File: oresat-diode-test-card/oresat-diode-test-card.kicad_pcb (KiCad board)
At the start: 4 copper layers, 99.8 x 94.6 mm, 123 parts, among them J6 J-SAMTEC-TFM-120-X1-XXX-D-RA, J7 ORESAT-DEBUG-CONNECTOR-ALL, Q1 DMP2240UDM, Q2 DMP3050LVT-7, Q4 DMP3050LVT-7, Q7 MOSFET-PCH-SOT23-6, Q8 PMV45EN, Q9 PMV45EN, U1 TCAN330, U10 TPS62111RSA, U11 MIC842LYC5, U12 MIC842LYC5, U2 MAX7310, U3 TS5A21366DCUR, U4 TLV6001DCK, U501 TLV6001DCK, U6 MAX4211, U7 STM32F091C, U8 NX3L4051-Q100, U9 TLV6001DCK, X2 CRYSTAL-WITH-GND

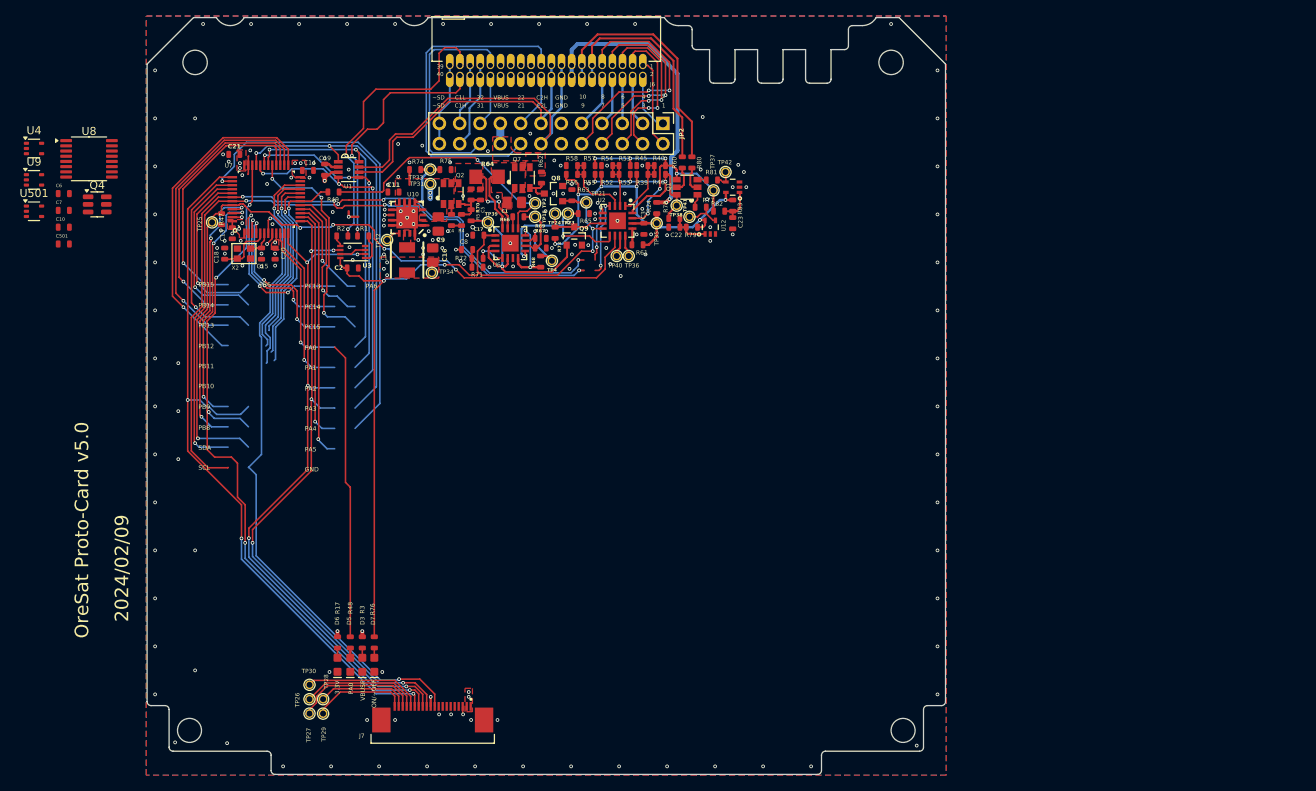
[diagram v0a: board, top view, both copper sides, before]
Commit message: started layout of components
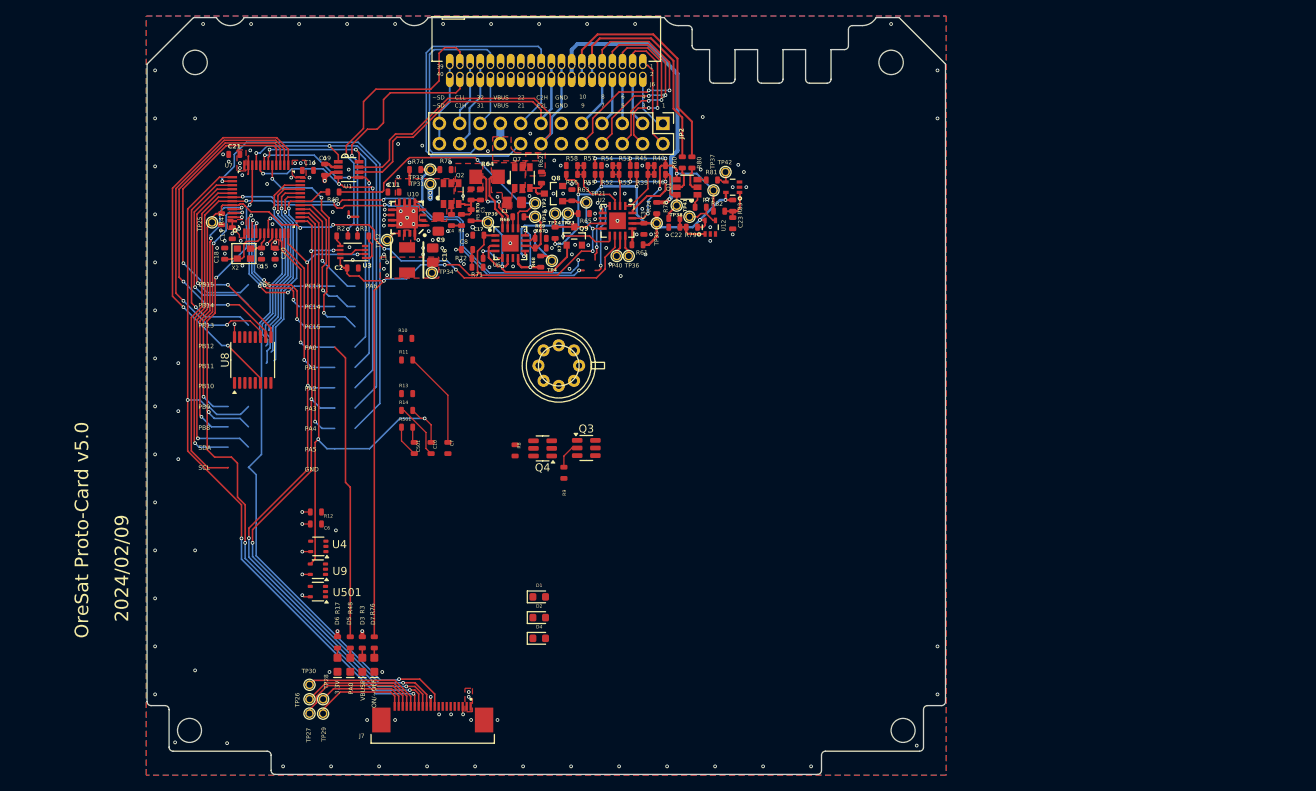
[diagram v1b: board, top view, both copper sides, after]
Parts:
- added D1: LED, oresat-diodes:LED_0603_1608Metric, F.Cu at (147.6, 130.1)
- added D2: LED, oresat-diodes:LED_0603_1608Metric, F.Cu at (147.6, 132.7)
- added D4: LED, oresat-diodes:LED_0603_1608Metric, F.Cu at (147.6, 135.3)
- added Q3: NMOS, Package_TO_SOT_SMD:SOT-23-6, F.Cu at (153.5, 111.5)
- added R10: 10K, oresat-passives:0603-C-NOSILK, F.Cu at (131.0, 97.8)
- added R11: 75, oresat-passives:0603-C-NOSILK, F.Cu at (131.1, 100.5)
- added R12: 0, oresat-passives:0603-C-NOSILK, F.Cu at (119.7, 119.5)
- added R13: 0, oresat-passives:0603-C-NOSILK, F.Cu at (131.1, 104.7)
- added R14: 10K, oresat-passives:0603-C-NOSILK, F.Cu at (131.1, 106.8)
- added R501: 10K, oresat-passives:0603-C-NOSILK, F.Cu at (131.1, 108.9)
- added R8: 10K, oresat-passives:0603-C-NOSILK, F.Cu at (144.6, 111.8)
- added R9: 10K, oresat-passives:0603-C-NOSILK, F.Cu at (150.7, 114.6)
- added U5: ~, oresat-diodes:MTMD142345PDT38, F.Cu at (150.1, 101.2)
- moved Q4 63.5 mm to (148.0, 111.5), turned to 180 degrees
- moved U4 61.1 mm to (120.0, 123.8), turned to 180 degrees
- moved U9 60.2 mm to (120.0, 126.7), turned to 180 degrees
- moved U501 59.3 mm to (120.0, 129.4), turned to 180 degrees
- moved C7 56.5 mm to (136.2, 111.5), turned to -90 degrees
- moved C10 53.6 mm to (134.1, 111.5), turned to -90 degrees
- moved C6 51.9 mm to (119.7, 121.0), turned to 180 degrees
- moved C501 50.7 mm to (132.0, 111.5), turned to -90 degrees
- moved U8 32.4 mm to (111.8, 100.5), turned to 90 degrees
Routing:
- net SWIR_PD_CURRENT: track 32.5 -> 66.7 mm, vias 1 -> 2
- net LED_CURRENT: track 21.1 -> 33.2 mm
- net LED_MUX_A2: track 32.2 -> 40.9 mm, vias 1 -> 2
- net SWIR_PD_C: track 0.00 -> 7.11 mm
- net 3.3V: track 9.65 -> 16.5 mm, vias 16 -> 22
- net LED_MUX_A1: track 36.0 -> 42.8 mm, vias 1 -> 2
- net ~{LED_MUX_ENABLE}: track 42.7 -> 49.0 mm, vias 1 -> 2
- net LED_MUX_A0: track 39.8 -> 45.5 mm, vias 1 -> 2
- net UV_PD_C: track 0.00 -> 3.96 mm
- net Net-(Q3-G): track 0.00 -> 3.48 mm
- net UV_PD_CURRENT: track 13.7 -> 15.7 mm
- net GND: vias 172 -> 163

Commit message: intial layout placed
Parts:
- added HW1: M2-Press-Fit-Nut, oresat-misc:M2-Press-Fit-Nut, F.Cu at (147.0, 131.6)
- added HW1: M2-Press-Fit-Nut, oresat-misc:M2-Press-Fit-Nut, F.Cu at (177.4, 113.5)
- added HW2: M2-Press-Fit-Nut, oresat-misc:M2-Press-Fit-Nut, F.Cu at (170.6, 131.6)
- added HW2: M2-Press-Fit-Nut, oresat-misc:M2-Press-Fit-Nut, F.Cu at (177.4, 89.9)
- D1, D2, D4: footprint oresat-diodes:LED_0603_1608Metric -> Diode_SMD:D_0201_0603Metric
- moved U9 57.9 mm to (172.6, 102.3)
- moved U8 39.6 mm to (147.0, 118.6), turned to 180 degrees
- moved U4 35.9 mm to (140.4, 94.2), turned to 90 degrees
- moved U501 35.6 mm to (155.5, 132.1)
- moved R501 32.0 mm to (155.2, 129.9), turned to 180 degrees
- moved C6 30.7 mm to (134.3, 94.0), turned to 90 degrees
- moved R12 30.4 mm to (136.2, 94.0), turned to 90 degrees
- moved C501 28.7 mm to (155.2, 128.4), turned to 0 degrees
- moved U5 27.9 mm to (178.0, 101.7), turned to 180 degrees
- moved Q3 14.7 mm to (144.8, 99.6), turned to 90 degrees
- moved D4 14.7 mm to (161.6, 130.9)
- moved D1 14.0 mm to (161.6, 128.8)
- moved D2 13.9 mm to (161.5, 132.8)
- moved C7 13.8 mm to (138.4, 97.9), turned to 90 degrees
- moved Q4 13.0 mm to (139.5, 101.7)
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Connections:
- U5 pad 1: (no net) -> GND
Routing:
- net 3.3V: track 16.5 -> 115.7 mm, vias 22 -> 16
- net unconnected-(U7-PB6-Pad42): track 91.3 -> 0.00 mm, vias 4 -> 0
- net unconnected-(U7-PB7-Pad43): track 88.8 -> 0.00 mm, vias 5 -> 0
- net Net-(D1-A): track 0.00 -> 77.5 mm, vias 0 -> 5
- net UV_PD_CURRENT: track 15.7 -> 84.6 mm, vias 1 -> 4
- net unconnected-(U7-PA15-Pad38): track 59.5 -> 0.00 mm, vias 1 -> 0
- net Net-(U5-1460nm): track 0.00 -> 48.6 mm, vias 0 -> 2
- net ~{LED_MUX_ENABLE}: track 49.0 -> 95.8 mm, vias 2 -> 4
- net LED_CURRENT: track 33.2 -> 79.6 mm, vias 1 -> 4
- net Net-(U5-1040nm): track 0.00 -> 46.3 mm, vias 0 -> 2
- net Net-(U5-1200nm): track 0.00 -> 44.8 mm, vias 0 -> 2
- net Net-(U5-1300nm): track 0.00 -> 44.6 mm, vias 0 -> 2
- net LED_MUX_A1: track 42.8 -> 86.4 mm, vias 2 -> 4
- net LED_MUX_A2: track 40.9 -> 84.3 mm, vias 2 -> 4
- net /Power/UART_EN: track 3.31 -> 46.2 mm, vias 0 -> 2
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
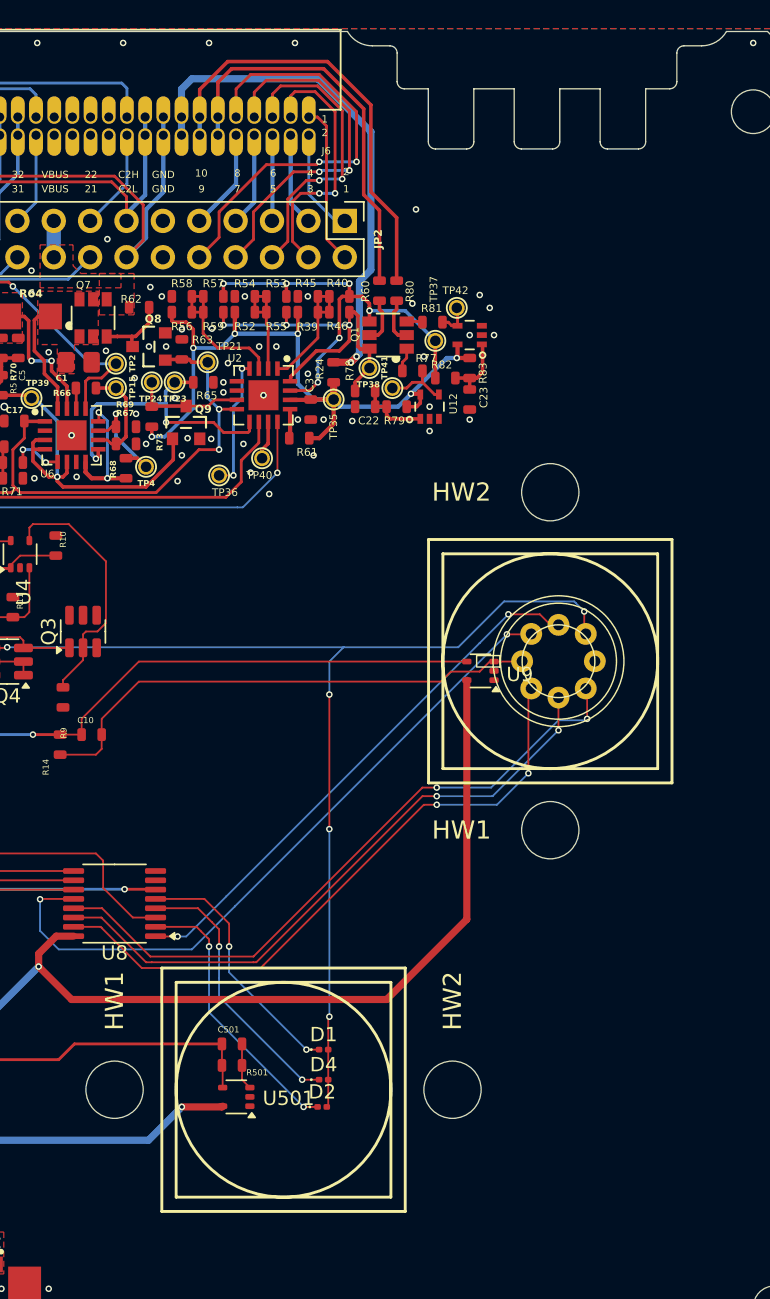
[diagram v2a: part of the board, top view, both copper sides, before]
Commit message: updated UV LED package type
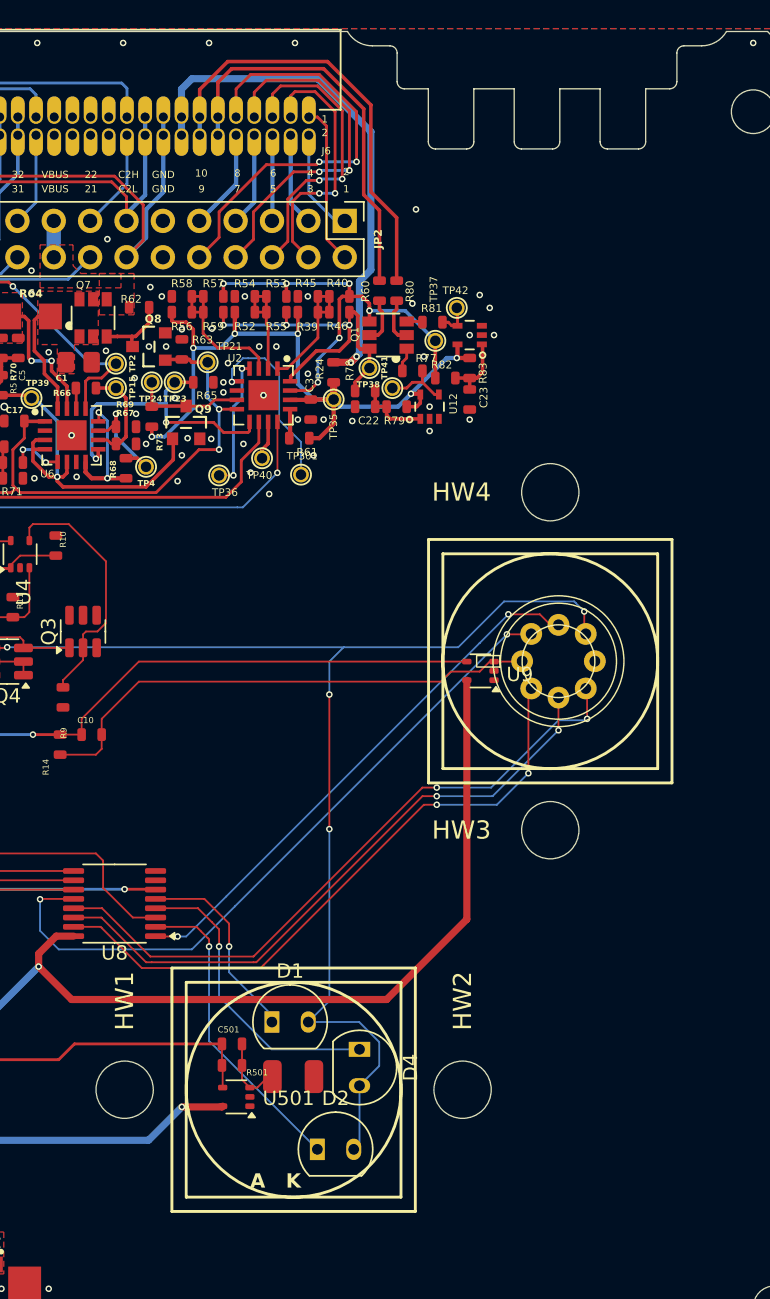
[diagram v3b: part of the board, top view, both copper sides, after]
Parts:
- added D8: D_Photo, oresat-diodes:GVBL-S12SD, F.Cu at (158.6, 130.7)
- added TP301: TEST-POINT-LARGE-SQUARE, oresat-proto-card:1X01, F.Cu at (160.0, 88.6)
- D1, D2, D4: footprint Diode_SMD:D_0201_0603Metric -> Package_TO_SOT_THT:TO-92-2
- moved D1 4.09 mm to (158.0, 126.9)
- moved D4 3.28 mm to (164.1, 128.8), turned to -90 degrees
- moved D2 2.98 mm to (161.2, 135.8)
- moved HW1 0.71 mm to (147.7, 131.6)
- moved HW2 0.71 mm to (171.3, 131.6)
- renumbered HW1 to HW3, HW2 to HW4
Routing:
- net Net-(U2-IO1): track 0.00 -> 13.0 mm, vias 0 -> 1
- net Net-(D1-A): track 77.5 -> 85.7 mm
- net Net-(D1-K): track 17.8 -> 14.0 mm
- net Net-(D2-K): track 19.5 -> 21.9 mm
- net Net-(D4-K): track 19.1 -> 21.1 mm
- net UV_PD_C: track 3.28 -> 5.06 mm
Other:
- board text added: "A K"

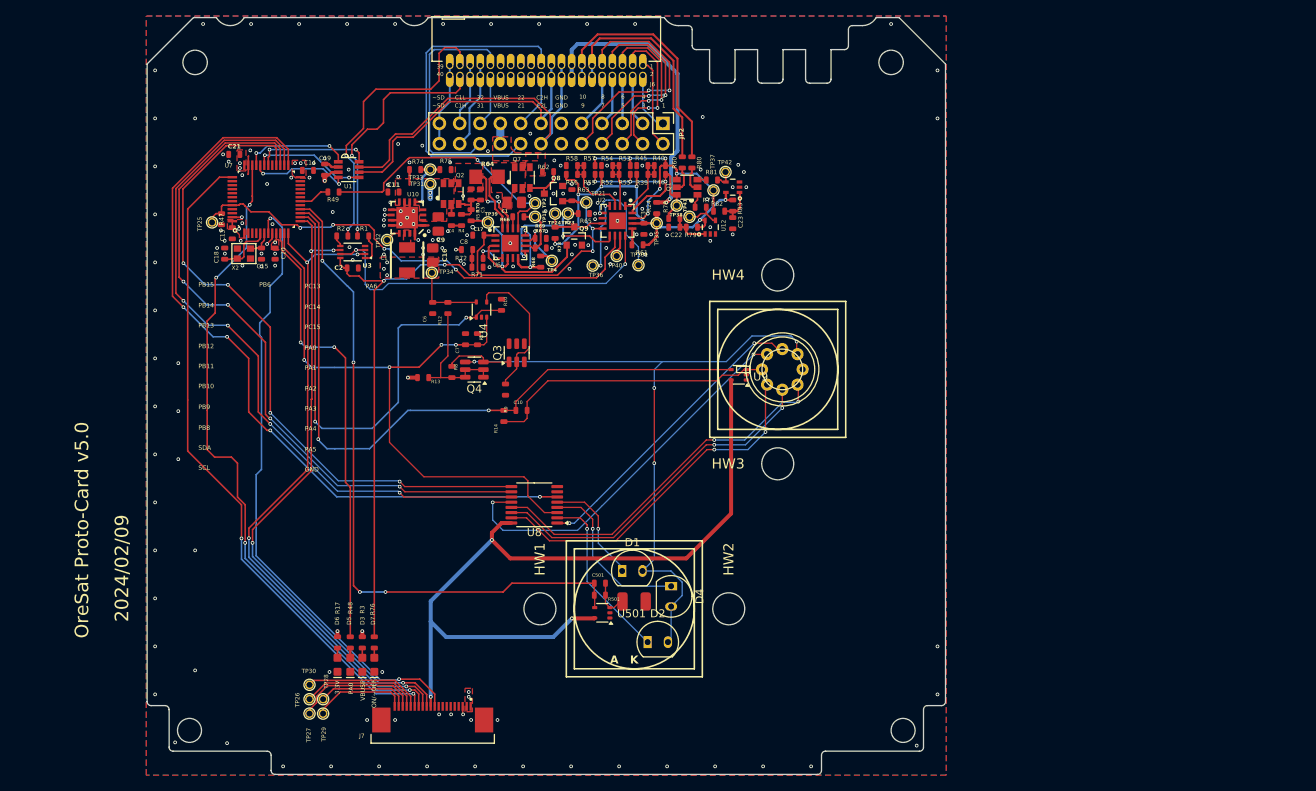
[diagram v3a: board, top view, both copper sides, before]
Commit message: updated layout and schematic with correct values
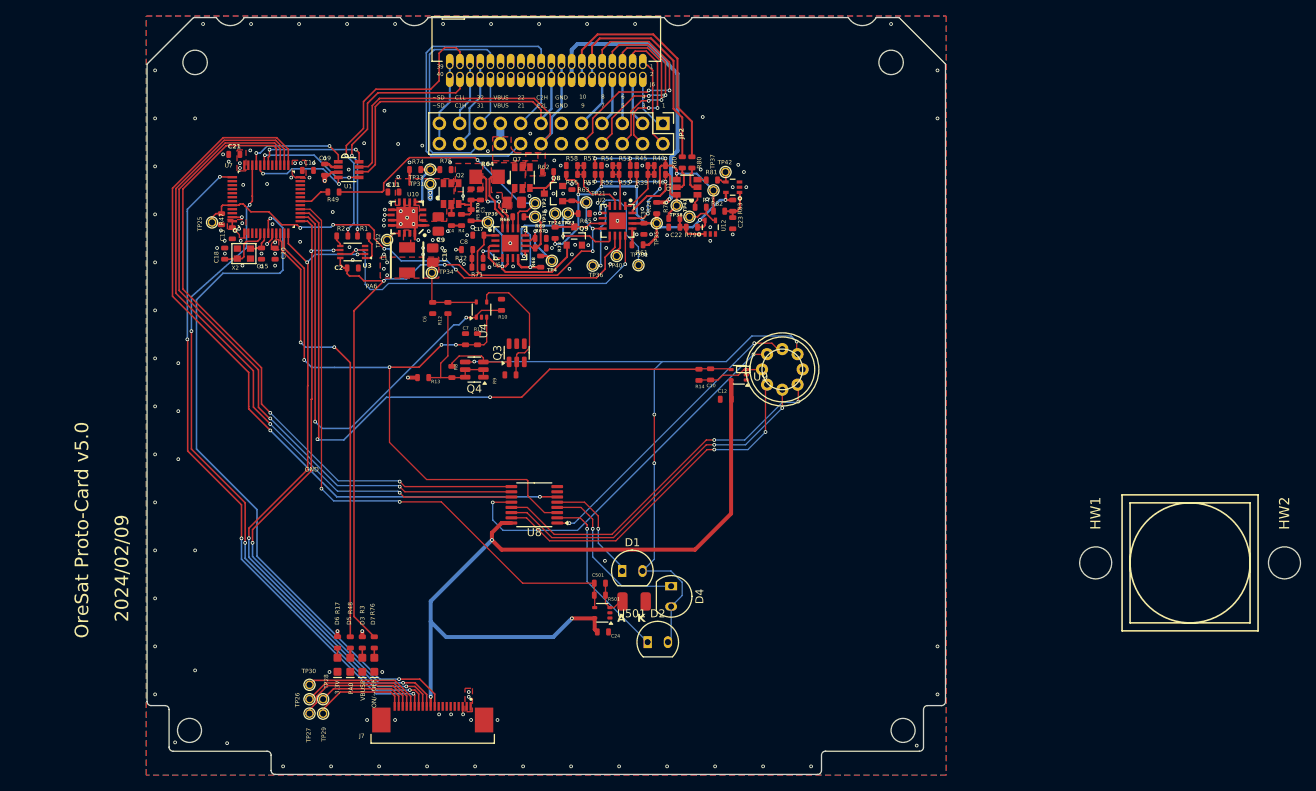
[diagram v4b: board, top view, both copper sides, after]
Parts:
- removed HW3, HW4: M2-Press-Fit-Nut, oresat-misc:M2-Press-Fit-Nut
- added C12: 100n, oresat-passives:0603-C-NOSILK, F.Cu at (170.9, 105.4)
- added C24: 100n, oresat-passives:0603-C-NOSILK, F.Cu at (155.6, 134.5)
- C6: value 100u -> 100n
- C7: value 100u -> 10u
- PCB1: value ORESAT-CARD-V1.3-3RF -> ORESAT-CARD-V1.0-0xRF; footprint oresat-pcbs:ORESAT-CARD-V1.3-3RF -> oresat-pcbs:ORESAT-CARD-V1.3-0RF
- moved HW1 69.7 mm to (217.2, 125.9)
- moved HW2 69.7 mm to (240.8, 125.9)
- moved R14 24.9 mm to (167.6, 102.4)
- moved C10 24.1 mm to (169.0, 102.3), turned to -90 degrees
- moved R9 1.94 mm to (144.0, 102.4), turned to 0 degrees
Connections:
- net SWIR_PD_C renamed Net-(U5-PD_Cathode)
- net UV_PD_C renamed Net-(D8-A)
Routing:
- net Net-(U5-PD_Cathode): track 36.2 -> 8.53 mm
- net /Microcontroller/NRESET: track 77.6 -> 87.9 mm
- net UV_PD_CURRENT: track 84.6 -> 78.8 mm, vias 4 -> 2
- net DAC_OUT: track 62.2 -> 56.8 mm
- net 3.3V: track 115.7 -> 119.1 mm
- net CAN2_L: track 37.8 -> 40.5 mm
- net CAN2_H: track 44.8 -> 47.5 mm
- net GND: track 23.9 -> 21.6 mm, vias 162 -> 166
- net /Power/ON/~{OFF}: track 98.8 -> 100.9 mm
- net LED_MUX_A2: track 84.3 -> 82.6 mm, vias 4 -> 2
- net Net-(Q3-G): track 17.9 -> 16.3 mm
- net LED_MUX_A1: track 86.4 -> 84.8 mm, vias 4 -> 2
- net LED_MUX_A0: track 88.3 -> 86.8 mm, vias 4 -> 2
- net SWIR_PD_CURRENT: track 86.9 -> 85.5 mm
- net ~{LED_MUX_ENABLE}: track 95.8 -> 94.5 mm, vias 4 -> 2
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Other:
- outline, holes or cut-outs redrawn
- board text removed: "PA1"
- board text removed: "PA2"
- board text removed: "PA3"
- board text removed: "PA4"
- board text removed: "PA5"
- board text removed: "PB10"
- board text removed: "PB11"
- board text removed: "PB12"
- board text removed: "PB13"
- board text removed: "PB14"
- board text removed: "PB15"
- board text removed: "PB6"
- board text removed: "PB8"
- board text removed: "PB9"
- board text removed: "PC13"
- board text removed: "PC14"
- board text removed: "PC15"
- board text removed: "SCL"
- board text removed: "SDA"

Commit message: second rought draft layout, fixed library issues
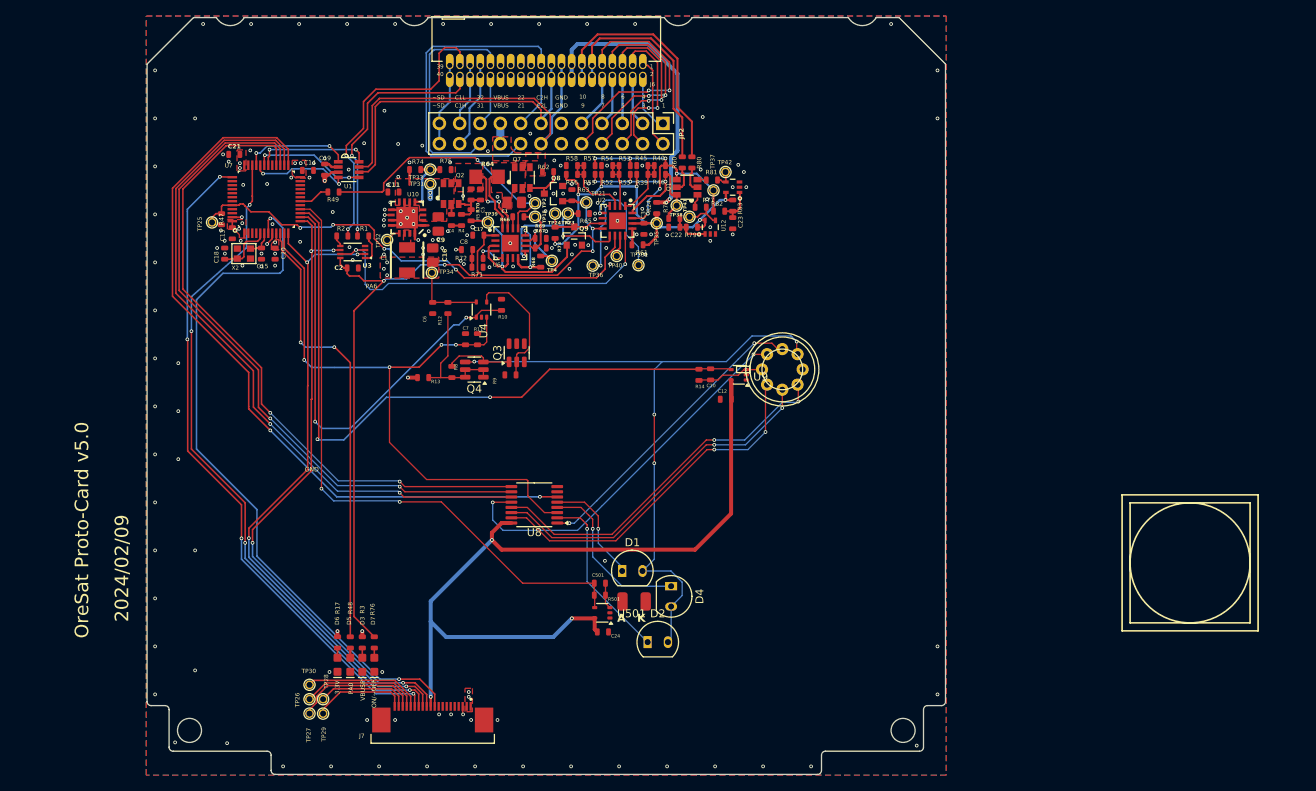
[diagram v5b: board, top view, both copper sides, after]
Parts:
- removed H2, H3: STAND-OFFTIGHT, oresat-proto-card:STAND-OFF-TIGHT
- removed HW1, HW2: M2-Press-Fit-Nut, oresat-misc:M2-Press-Fit-Nut
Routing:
- net Net-(D8-K): track 5.06 -> 3.28 mm
